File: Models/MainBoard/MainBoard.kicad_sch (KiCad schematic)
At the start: 0 parts

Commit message: Save progress
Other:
- sheet DAC1: file DAC.kicad_sch -> DAC1.kicad_sch
- sheet DAC2: file DAC.kicad_sch -> DAC2.kicad_sch
- note added: "DAC1: - fine X - fine Y - fine Z - coarse Z four channels, ±12 V (mode 1110)"
- note added: "DAC2: - piezo voltage (Phase 0.2) - bias voltage (Phase II) single channel, ±12 V (mode 1110)"
- note added: "Input: - 100 MΩ or 330 MΩ - switched by PCB swapping - design for 330 MΩ - debug with 100 MΩ single channel, ±12.288 V (mode 0000)"
- note removed: "DAC1: - fine X - fine Y - fine Z - coarse Z all channels ±12 V (mode 1110)"
- note removed: "DAC2: - piezo voltage (Phase 0.2) - bias voltage (Phase II) ±12 V (mode 1110)"
- note removed: "Input: - 100 MΩ or 330 MΩ - switched by PCB swapping - design for 330 MΩ - debug with 100 MΩ ±12.288 V (mode 0000)"
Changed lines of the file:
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@@
 	(generator_version "9.0")
 	(paper "A4")
-	(text "DAC2:\n- piezo voltage (Phase 0.2)\n- bias voltage (Phase II)\n\n±12 V (mode 1110)"
+	(text "DAC2:\n- piezo voltage (Phase 0.2)\n- bias voltage (Phase II)\n\nsingle channel, ±12 V (mode 1110)"
 		(exclude_from_sim no)
 		(at 86.868 64.77 0)
@@
 		)
 	)
-	(text "DAC1:\n- fine X\n- fine Y\n- fine Z\n- coarse Z\n\nall channels ±12 V (mode 1110)\n"
+	(text "DAC1:\n- fine X\n- fine Y\n- fine Z\n- coarse Z\n\nfour channels, ±12 V (mode 1110)\n"
 		(exclude_from_sim no)
 		(at 86.106 26.162 0)
@@
 		)
 	)
-	(text "Input:\n- 100 MΩ or 330 MΩ\n- switched by PCB swapping\n- design for 330 MΩ\n- debug with 100 MΩ\n\n±12.288 V (mode 0000)"
+	(text "Input:\n- 100 MΩ or 330 MΩ\n- switched by PCB swapping\n- design for 330 MΩ\n- debug with 100 MΩ\n\nsingle channel, ±12.288 V (mode 0000)"
 		(exclude_from_sim no)
 		(at 86.106 105.156 0)
@@
 	)
 	(sheet
+		(at 127 63.5)
+		(size 25.4 25.4)
+		(exclude_from_sim no)
+		(in_bom yes)
+		(on_board yes)
+		(dnp no)
+		(fields_autoplaced yes)
+		(stroke
+			(width 0.1524)
+			(type solid)
+		)
+		(fill
+			(color 0 0 0 0.0000)
+		)
+		(property "Sheetname" "DAC2"
+			(at 127 62.7884 0)
+			(effects
+				(font
+					(size 1.27 1.27)
+				)
+				(justify left bottom)
+			)
+		)
+		(property "Sheetfile" "DAC2.kicad_sch"
+			(at 127 89.4846 0)
+			(effects
+				(font
+					(size 1.27 1.27)
+				)
+				(justify left top)
+			)
+		)
+		(instances
+			(project "MainBoard"
+				(path "/600cc1cc-74ca-4bfc-97a0-b230eb3afbcd"
+					(page "7")
+				)
+			)
+		)
+	)
+	(sheet
 		(at 127 139.7)
 		(size 25.4 25.4)
@@
 	)
 	(sheet
-		(at 127 63.5)
-		(size 25.4 25.4)
-		(exclude_from_sim no)
-		(in_bom yes)
-		(on_board yes)
-		(dnp no)
-		(fields_autoplaced yes)
-		(stroke
-			(width 0.1524)
-			(type solid)
-		)
-		(fill
-			(color 0 0 0 0.0000)
-		)
-		(property "Sheetname" "DAC2"
-			(at 127 62.7884 0)
-			(effects
-				(font
-					(size 1.27 1.27)
-				)
-				(justify left bottom)
-			)
-		)
-		(property "Sheetfile" "DAC.kicad_sch"
-			(at 127 89.4846 0)
-			(effects
-				(font
-					(size 1.27 1.27)
-				)
-				(justify left top)
-			)
-		)
-		(instances
-			(project "MainBoard"
-				(path "/600cc1cc-74ca-4bfc-97a0-b230eb3afbcd"
-					(page "5")
-				)
-			)
-		)
-	)
-	(sheet
 		(at 127 25.4)
 		(size 25.4 25.4)
@@
 			)
 		)
-		(property "Sheetfile" "DAC.kicad_sch"
+		(property "Sheetfile" "DAC1.kicad_sch"
 			(at 127 51.3846 0)
 			(effects

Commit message: Save progress
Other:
- note added: "DAC1: - fine X - fine Y - fine Z - coarse Z four channels, ±12 V (mode 1110) ±15 mA current drive"
- note added: "DAC2: - piezo voltage (Phase 0.2) - bias voltage (Phase II) single channel, ±12 V (mode 1110) ±2.5 mA current drive"
- note removed: "DAC1: - fine X - fine Y - fine Z - coarse Z four channels, ±12 V (mode 1110)"
- note removed: "DAC2: - piezo voltage (Phase 0.2) - bias voltage (Phase II) single channel, ±12 V (mode 1110)"
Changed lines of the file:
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@@
 	(generator_version "9.0")
 	(paper "A4")
-	(text "DAC2:\n- piezo voltage (Phase 0.2)\n- bias voltage (Phase II)\n\nsingle channel, ±12 V (mode 1110)"
+	(text "DAC2:\n- piezo voltage (Phase 0.2)\n- bias voltage (Phase II)\n\nsingle channel, ±12 V (mode 1110)\n±2.5 mA current drive"
 		(exclude_from_sim no)
-		(at 86.868 64.77 0)
+		(at 86.614 64.77 0)
 		(effects
 			(font
@@
 		)
 	)
-	(text "DAC1:\n- fine X\n- fine Y\n- fine Z\n- coarse Z\n\nfour channels, ±12 V (mode 1110)\n"
+	(text "DAC1:\n- fine X\n- fine Y\n- fine Z\n- coarse Z\n\nfour channels, ±12 V (mode 1110)\n±15 mA current drive\n"
 		(exclude_from_sim no)
 		(at 86.106 26.162 0)

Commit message: Save progress
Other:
- note added: "DAC1: - fine X - fine Y - fine Z - coarse Z four channels, ±12 V (mode 1110)"
- note removed: "DAC1: - fine X - fine Y - fine Z - coarse Z four channels, ±12 V (mode 1110) ±15 mA current drive"
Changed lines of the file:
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@@
 		)
 	)
-	(text "DAC1:\n- fine X\n- fine Y\n- fine Z\n- coarse Z\n\nfour channels, ±12 V (mode 1110)\n±15 mA current drive\n"
+	(text "DAC1:\n- fine X\n- fine Y\n- fine Z\n- coarse Z\n\nfour channels, ±12 V (mode 1110)"
 		(exclude_from_sim no)
 		(at 86.106 26.162 0)

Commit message: Save progress
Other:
- sheet ADC ports: added AIN_GND, AIN_P, CS, MISO, MOSI, SCK; removed none
- sheet CDC ports: added CIN, EXC, SCL, SDA; removed none
- sheet DAC1 ports: added CS, MISO, MOSI, OUTA, OUTB, OUTC, OUTD, SCK, SENSENA, SENSENB, SENSENC, SENSEND; removed none
- sheet DAC2 ports: added CS, MISO, MOSI, Output, SCK, SENSEN; removed none
- sheet Isolation ports: added 3.3V_Analog, 3.3V_Digital, 5V_Analog, CS1_Analog, CS1_Digital, CS2_Analog, CS2_Digital, CS3_Analog, CS3_Digital, GND_Analog, GND_Digital, MISO_Analog, MISO_Digital, MOSI_Analog, MOSI_Digital, SCK_Analog, SCK_Digital, SCL_Analog, SCL_Digital, SDA_Analog, SDA_Digital; removed none
- note added: "Output: - fine X - fine Y - fine Z - coarse Z four channels, ±12 V (mode 1110)"
- note added: "Output: - piezo voltage (Phase 0.2) - bias voltage (Phase II) single channel, ±12 V (mode 1110) ±2.5 mA current drive"
- note added: "TODO: - power & GND receptacles to power board - signal receptacles"
- note removed: "DAC1: - fine X - fine Y - fine Z - coarse Z four channels, ±12 V (mode 1110)"
- note removed: "DAC2: - piezo voltage (Phase 0.2) - bias voltage (Phase II) single channel, ±12 V (mode 1110) ±2.5 mA current drive"

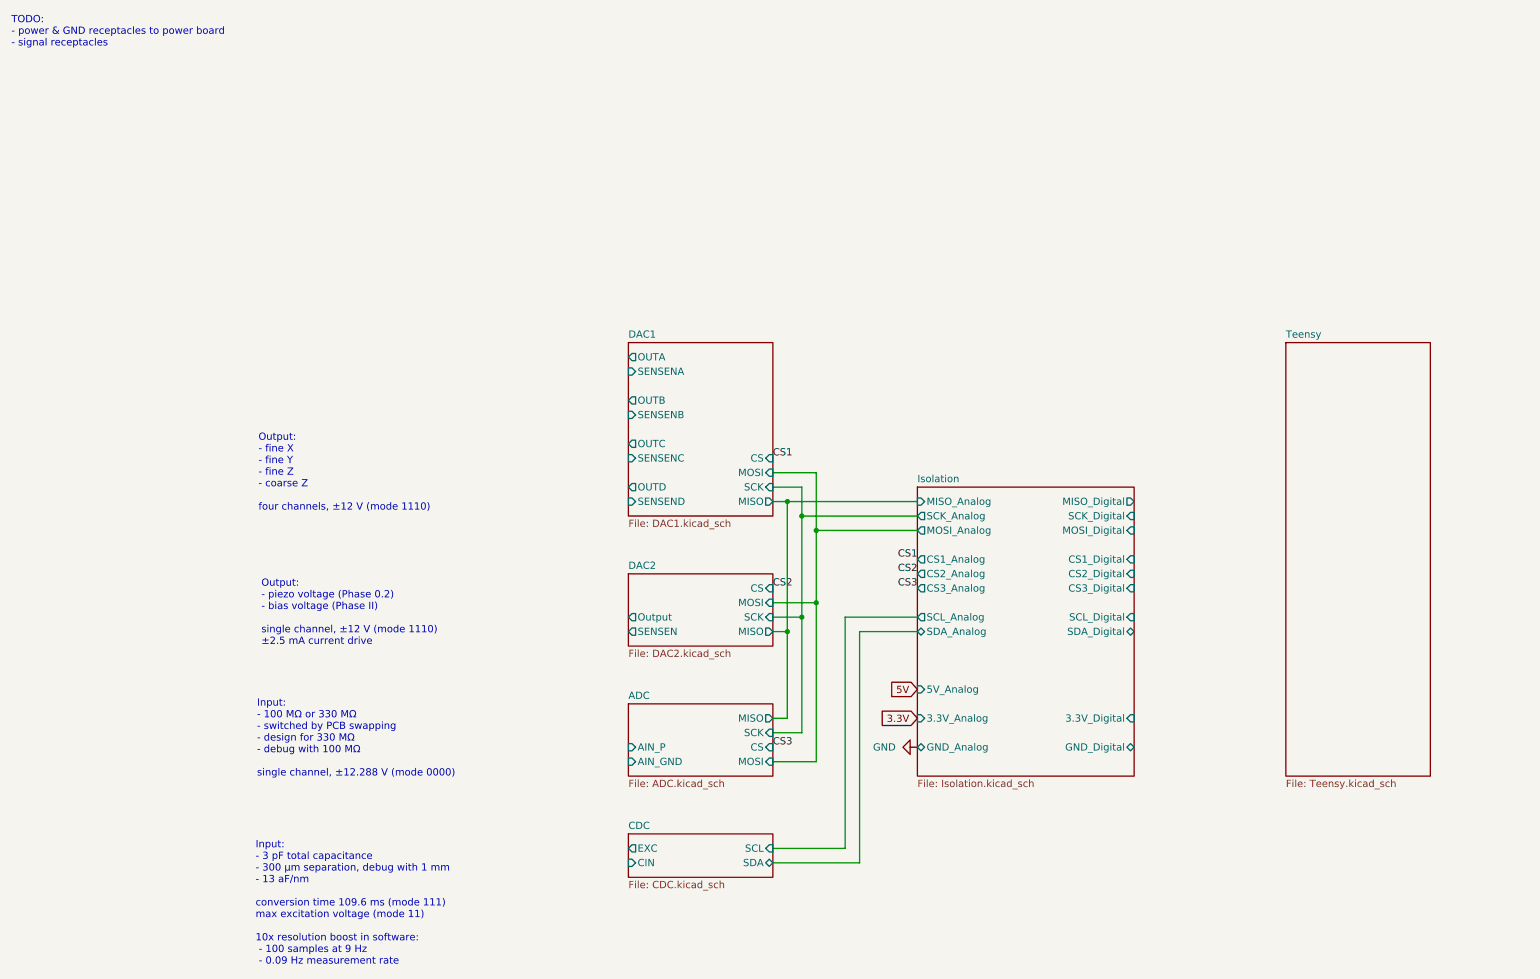
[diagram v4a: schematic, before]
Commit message: Added mounting holes
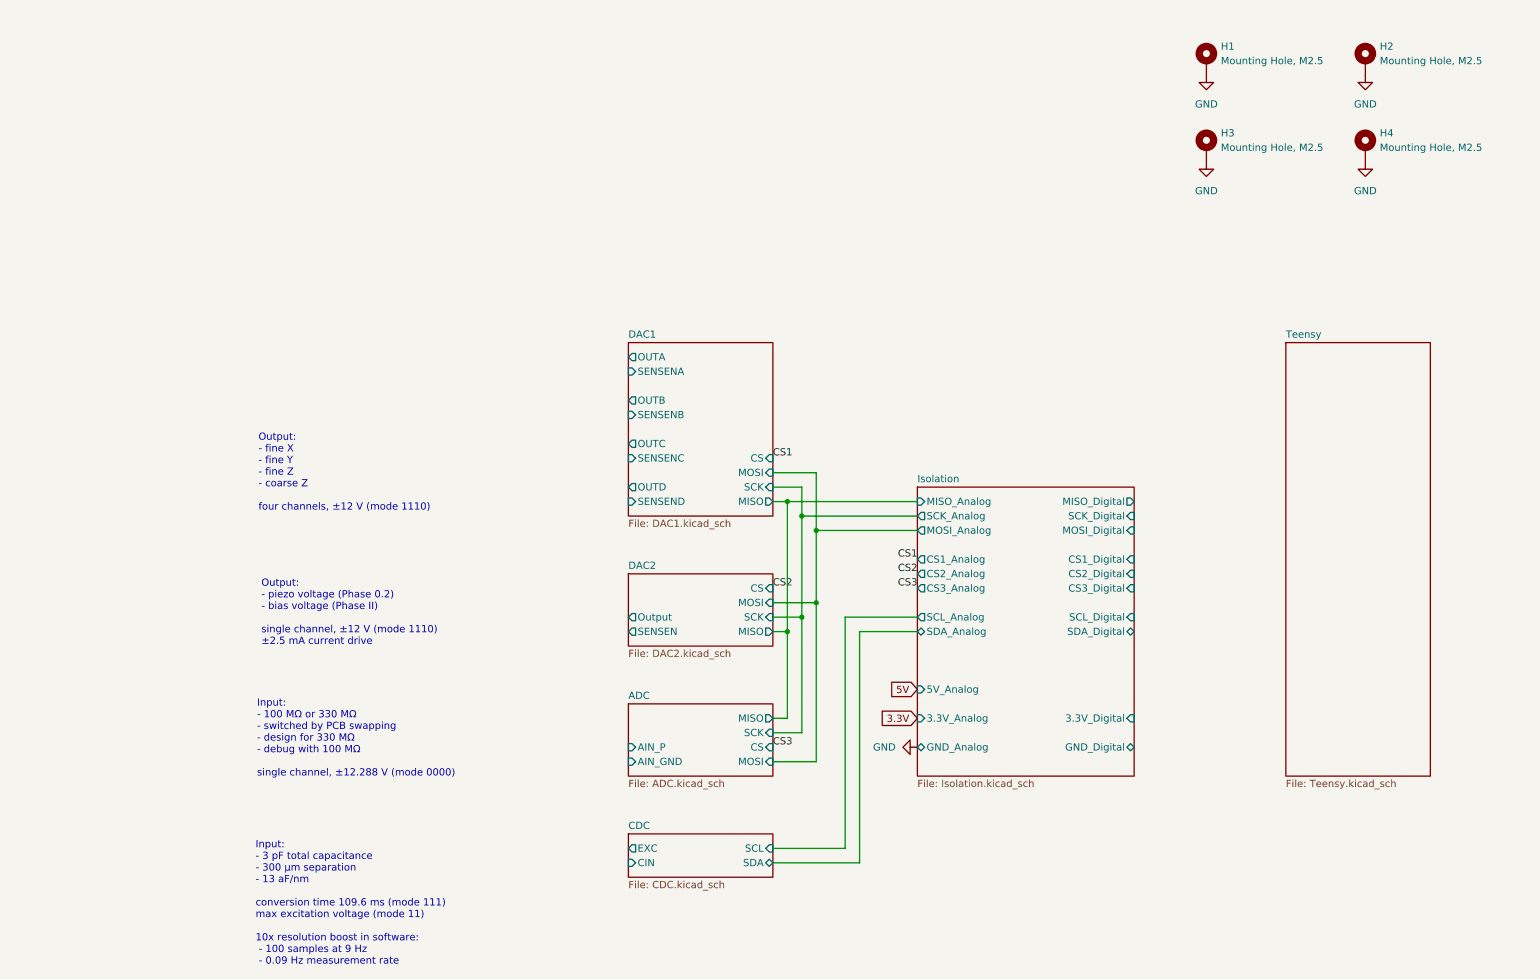
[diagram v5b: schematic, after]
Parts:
- added H1, H2, H3, H4: Mounting Hole, M2.5, MountingHole:MountingHole_2.7mm_M2.5_DIN965_Pad, symbol Mechanical:MountingHole_Pad
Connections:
- net GND: now also H1.1, H2.1, H3.1, H4.1
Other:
- note added: "Input: - 3 pF total capacitance - 300 μm separation - 13 aF/nm conversion time 109.6 ms (mode 111) max excitation voltage (mode 11) 10x resolution boost in software: - 100 samples at 9 Hz - 0.09 Hz measurement rate"
- note removed: "Input: - 3 pF total capacitance - 300 μm separation, debug with 1 mm - 13 aF/nm conversion time 109.6 ms (mode 111) max excitation voltage (mode 11) 10x resolution boost in software: - 100 samples at 9 Hz - 0.09 Hz measurement rate"
- note removed: "TODO: - power & GND receptacles to power board - signal receptacles"

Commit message: Save progress
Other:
- note added: "output voltage receptacle type: (1) SMA (2) 1x3 pin socket, GND + OUT + GND"
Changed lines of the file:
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@@
+		)
+	)
+	(text "output voltage receptacle type:\n(1) SMA\n(2) 1x3 pin socket, GND + OUT + GND"
+		(exclude_from_sim no)
+		(at 25.908 26.67 0)
+		(effects
+			(font
+				(size 1.27 1.27)
+			)
+			(justify left top)
 		)
 	)

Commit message: Save progress
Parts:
- added J10, J12, J14, J6, J8: Conn_01x03_Socket, symbol Connector:Conn_01x03_Socket
- added J11, J13, J5, J7, J9: Conn_Coaxial, symbol Connector:Conn_Coaxial
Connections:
- net GND: now also J10.1 (Pin_1), J10.3 (Pin_3), J11.2 (Ext), J12.1 (Pin_1), J12.3 (Pin_3), J13.2 (Ext), J14.1 (Pin_1), J14.3 (Pin_3), J5.2 (Ext), J6.1 (Pin_1), J6.3 (Pin_3), J7.2 (Ext), J8.1 (Pin_1), J8.3 (Pin_3), J9.2 (Ext)
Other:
- sheet DAC2 ports: added none; removed SENSEN
- note removed: "output voltage receptacle type: (1) SMA (2) 1x3 pin socket, GND + OUT + GND"

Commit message: Save progress
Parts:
- added J15: Conn_Coaxial, symbol Connector:Conn_Coaxial
- added J16: Conn_01x03_Socket, symbol Connector:Conn_01x03_Socket
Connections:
- net GND: now also J15.2 (Ext), J16.1 (Pin_1), J16.3 (Pin_3)
- net ADC_GND: now reaches J12.2 (Pin_2)
- net ADC_GND: now also J11.1 (In)
- net ADC_IN: now reaches J10.2 (Pin_2)
- net ADC_IN: now also J9.1 (In)
- net BIAS_OUT: now reaches J6.2 (Pin_2)
- net BIAS_OUT: now also J5.1 (In)
- net CDC_EXC: now reaches J13.1 (In)
- net CDC_EXC: now also J14.2 (Pin_2)
- net BIAS_GND: now reaches J7.1 (In)
- net BIAS_GND: now also J8.2 (Pin_2)
- new net CDC_CIN: J15.1 (In), J16.2 (Pin_2)
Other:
- sheet DAC2 ports: added SENSEN; removed none
- moved on the sheet: H1, H2, H3, H4
